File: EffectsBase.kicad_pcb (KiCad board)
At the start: 2 copper layers, 0 parts

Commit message: Initial schematic
Finished the base schematic.
Included all the controls and updated the power supply.
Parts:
- added REF**: Hammond_125B_1590N1_NOLID, Enclosures:Hammond_125B_1590N1_NOLID, B.Cu at (150.0, 100.0)
- added X1: PEDAL_COMBO_TOP, Custom_Parts:PEDAL_COMBO_TOP, F.Cu at (150.0, 44.0)
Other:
- board outline added: 59 x 95 mm
- copper layers 2 -> 4

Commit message: Initial layout
Finished the initial PCB layout.
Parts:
- removed X1: PEDAL_COMBO_TOP, Custom_Parts:PEDAL_COMBO_TOP
- added C1: 10u, Capacitor_SMD:C_0805_2012Metric, F.Cu at (94.8, 138.8)
- added C2: 10u, Capacitor_SMD:C_0805_2012Metric, F.Cu at (94.8, 141.2)
- added C3: 10n, Capacitor_SMD:C_0603_1608Metric, F.Cu at (87.2, 117.6)
- added C4: 10u, Capacitor_SMD:C_0805_2012Metric, F.Cu at (90.0, 134.4)
- added C5: 10u, Capacitor_SMD:C_0805_2012Metric, F.Cu at (90.0, 125.0)
- added C6: 10u, Capacitor_SMD:C_0805_2012Metric, F.Cu at (90.0, 127.8)
- added C7: 10u, Capacitor_SMD:C_0805_2012Metric, F.Cu at (90.0, 147.8)
- added C8: 10u, Capacitor_SMD:C_0805_2012Metric, F.Cu at (90.0, 145.6)
- added D1: SMF10CA, Diode_SMD:D_SOD-123F, F.Cu at (91.4, 117.6)
- added D2: MMSZ5248B, Diode_SMD:D_SOD-323, F.Cu at (88.0, 122.0)
- added D3: B5819W, Diode_SMD:D_SOD-123, F.Cu at (85.6, 140.0)
- added D4: H15VSD3B, Diode_SMD:D_SOD-323, F.Cu at (143.4, 67.2)
- added D5: H15VSD3B, Diode_SMD:D_SOD-323, F.Cu at (156.6, 67.2)
- added FB1: 850, Inductor_SMD:L_0603_1608Metric, F.Cu at (87.4, 126.4)
- added J1: JACK CONNECTOR, Custom_Parts:HEADER_THROUGH_2x03_P2.54mm, F.Cu at (150.0, 63.2)
- added J2: FOOTSWITCH, Custom_Parts:HEADER_THROUGH_2x06_P2.54mm, F.Cu at (150.0, 135.2)
- added J3: PCIE_FX, Custom_Parts:Mini PCI_Express, F.Cu at (150.0, 122.0)
- added Q1: SI2301BDS, Package_TO_SOT_SMD:SOT-23, F.Cu at (91.4, 122.0)
- added R1: 100, Resistor_SMD:R_0603_1608Metric, F.Cu at (90.0, 130.8)
- added R2: 4.7K, Resistor_SMD:R_0603_1608Metric, F.Cu at (89.2, 117.6)
- added RV1: RK09L, Custom_Parts:POT_SINGLE_VERTICAL_6X15, B.Cu at (170.0, 55.0)
- added RV2: RK09L, Custom_Parts:POT_SINGLE_VERTICAL_6X15, B.Cu at (150.0, 55.0)
- added RV3: RK09L, Custom_Parts:POT_SINGLE_VERTICAL_6X15, B.Cu at (130.0, 55.0)
- added RV4: RK09L, Custom_Parts:POT_SINGLE_VERTICAL_6X15, B.Cu at (150.0, 83.0)
- added SW1: SW_SPDT, Custom_Parts:SW_SPDT, B.Cu at (170.0, 83.0)
- added SW2: SW_SPDT, Custom_Parts:SW_SPDT, B.Cu at (130.0, 83.0)
- added SW3: MINI_SW, Custom_Parts:MINI_TOGGLE_SHIELD, B.Cu at (139.0, 105.0)
- added SW4: MINI_SW, Custom_Parts:MINI_TOGGLE_SHIELD, B.Cu at (161.0, 105.0)
- added U1: ICL7660S, Package_SO:SOIC-8_3.9x4.9mm_P1.27mm, F.Cu at (90.0, 140.0)
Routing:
- net /Controls/AUDIO_OUT: track 0.00 -> 100.1 mm, vias 0 -> 1
- net /Controls/AUDIO_IN: track 0.00 -> 100.1 mm, vias 0 -> 1
- net GND: track 0.00 -> 63.6 mm
- net +VCC_FILT: track 0.00 -> 19.2 mm
- net /Controls/FX_IN: track 0.00 -> 15.9 mm, vias 0 -> 2
- net /Controls/FX_OUT: track 0.00 -> 15.8 mm, vias 0 -> 2
- net /Controls/SW3_IN: track 0.00 -> 3.40 mm
- added copper zone on F.Cu, net +VCC
- added copper zone on F.Cu, net +VCC_FILT
- added copper zone on F.Cu, net +VDC
- added copper zone on F.Cu, net +VDC_PROT
- added copper zone on F.Cu, net -VSS
- added copper zone on F.Cu, net /Power/CAP+
- added copper zone on F.Cu, net /Power/CAP-
- added copper zone on F.Cu, net /Power/VG
- added copper zone on B.Cu, net GND
- added copper zone on F.Cu, net GND
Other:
- board size 59 x 95 mm -> 59 x 98 mm
- copper layers 4 -> 2
- board text added: "FOOTSWITCH 1"
- board text added: "FOOTSWITCH 2"

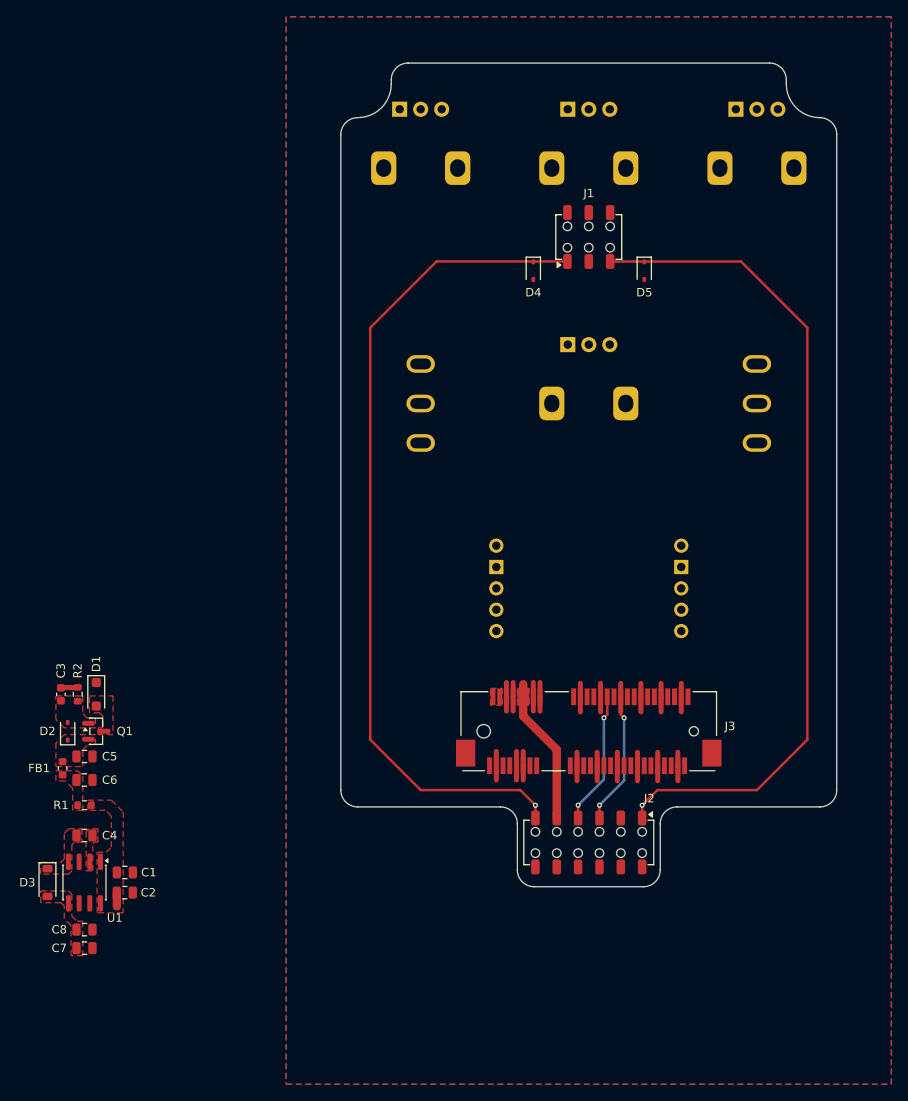
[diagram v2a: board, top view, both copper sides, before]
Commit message: Filtering section and layout
Updated the PCB layout.
Added additional input voltage filtering.
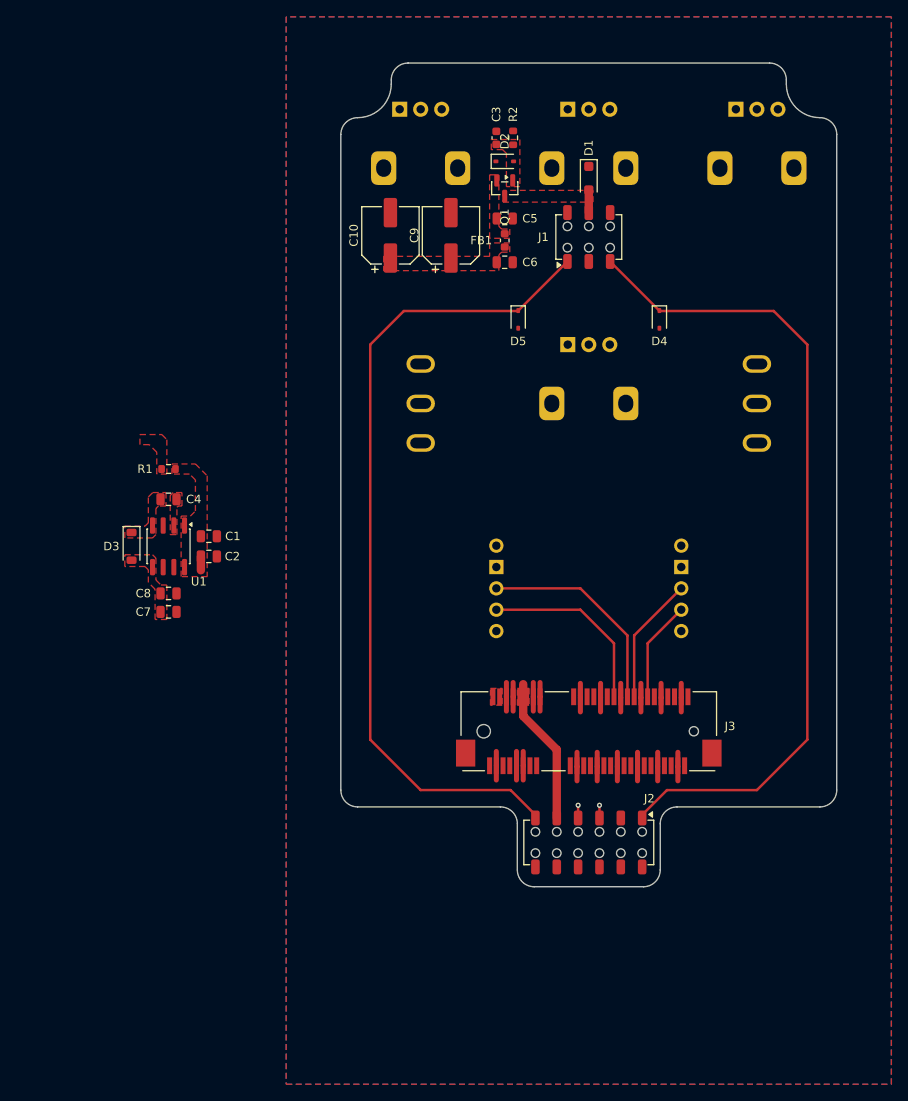
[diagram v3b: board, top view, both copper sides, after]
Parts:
- removed REF**: Hammond_125B_1590N1_NOLID, Enclosures:Hammond_125B_1590N1_NOLID
- added C10: 100u, Capacitor_SMD:CP_Elec_6.3x5.8, F.Cu at (126.4, 63.0)
- added C9: 100u, Capacitor_SMD:CP_Elec_6.3x5.8, F.Cu at (133.6, 63.0)
- moved D2 85.4 mm to (140.0, 54.2), turned to 0 degrees
- moved D1 84.9 mm to (150.0, 56.2)
- moved C3 84.1 mm to (139.0, 51.4)
- moved R2 84.1 mm to (141.0, 51.4)
- moved FB1 81.9 mm to (140.0, 63.6)
- moved C5 81.2 mm to (140.0, 61.0)
- moved Q1 80.8 mm to (140.0, 57.4), turned to -90 degrees
- moved C6 79.3 mm to (140.0, 66.2)
- moved C1 41.2 mm to (104.8, 98.8)
- moved C7 41.2 mm to (100.0, 107.8)
- moved R1 41.2 mm to (100.0, 90.8)
- moved C4 41.2 mm to (100.0, 94.4)
- moved C8 41.2 mm to (100.0, 105.6)
- moved D3 41.2 mm to (95.6, 100.0)
- moved U1 41.2 mm to (100.0, 100.0)
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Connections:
- J3 pad 30: /Controls/SW3_IN -> /Controls/SW3_NO
- J3 pad 34: /Controls/SW3_NO -> /Controls/SW3_IN
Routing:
- net /Controls/SW3_NO: track 0.00 -> 22.0 mm
- net /Controls/SW3_IN: track 3.40 -> 25.2 mm
- net /Controls/SW4_IN: track 0.00 -> 15.2 mm
- net /Controls/FX_IN: track 15.9 -> 1.52 mm, vias 2 -> 1
- net /Controls/FX_OUT: track 15.8 -> 1.52 mm, vias 2 -> 1
- net /Controls/SW4_NO: track 0.00 -> 12.0 mm
- net +VDC: track 0.00 -> 2.69 mm
- net /Controls/AUDIO_IN: track 100.1 -> 98.3 mm, vias 1 -> 0
- net /Controls/AUDIO_OUT: track 100.1 -> 98.3 mm, vias 1 -> 0
- net GND: track 63.6 -> 65.1 mm

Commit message: Charge pump layout
Added the layout for the charge pump.
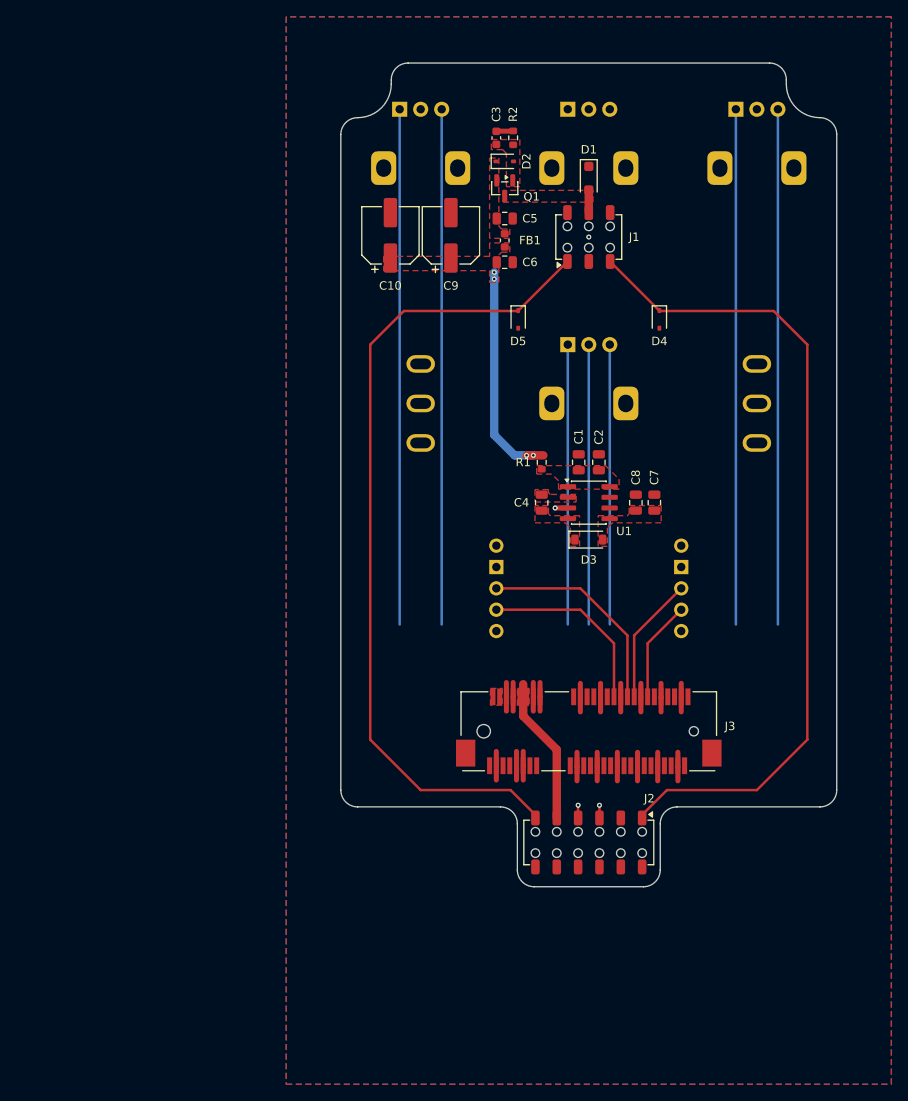
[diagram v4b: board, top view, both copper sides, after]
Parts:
- moved C7 59.2 mm to (157.8, 94.8), turned to 90 degrees
- moved C8 56.6 mm to (155.6, 94.8), turned to 90 degrees
- moved D3 54.4 mm to (150.0, 99.2), turned to 0 degrees
- moved U1 50.3 mm to (150.0, 94.8), turned to 0 degrees
- moved C2 47.7 mm to (151.2, 90.0), turned to 90 degrees
- moved C1 44.9 mm to (148.8, 90.0), turned to 90 degrees
- moved R1 44.4 mm to (144.4, 90.0), turned to -90 degrees
- moved C4 44.4 mm to (144.4, 94.8), turned to -90 degrees
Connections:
- C3 pad 2: GND -> +VCC
- J3 pad 11: GND -> +VCC
- J3 pad 14: GND -> +VCC
- J3 pad 16: GND -> +VCC
- J3 pad 19: GND -> +VCC
- J3 pad 20: GND -> +VCC
- J3 pad 25: GND -> +VCC
- J3 pad 26: GND -> +VCC
- J3 pad 3: GND -> +VCC
- J3 pad 31: GND -> +VCC
- J3 pad 32: GND -> +VCC
- J3 pad 37: GND -> +VCC
- J3 pad 38: GND -> +VCC
- J3 pad 43: GND -> +VCC
- J3 pad 44: GND -> +VCC
- J3 pad 49: GND -> +VCC
- J3 pad 50: GND -> +VCC
- J3 pad 6: GND -> +VCC
- J3 pad 8: GND -> +VCC
- J3 pad 9: GND -> +VCC
- R2 pad 2: GND -> +VCC
- U1 pad 3: GND -> +VCC
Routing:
- net +VCC: track 0.00 -> 95.6 mm, vias 0 -> 4
- net GND: track 65.1 -> 0.00 mm, vias 0 -> 2
- net /Controls/P3_L: track 0.00 -> 61.3 mm
- net /Controls/P3_H: track 0.00 -> 61.3 mm
- net /Controls/P1_L: track 0.00 -> 61.3 mm
- net /Controls/P1_H: track 0.00 -> 61.3 mm
- net /Controls/P4_W: track 0.00 -> 33.3 mm
- net /Controls/P4_L: track 0.00 -> 33.3 mm
- net /Controls/P4_H: track 0.00 -> 33.3 mm
- net +VCC_FILT: track 19.2 -> 17.6 mm

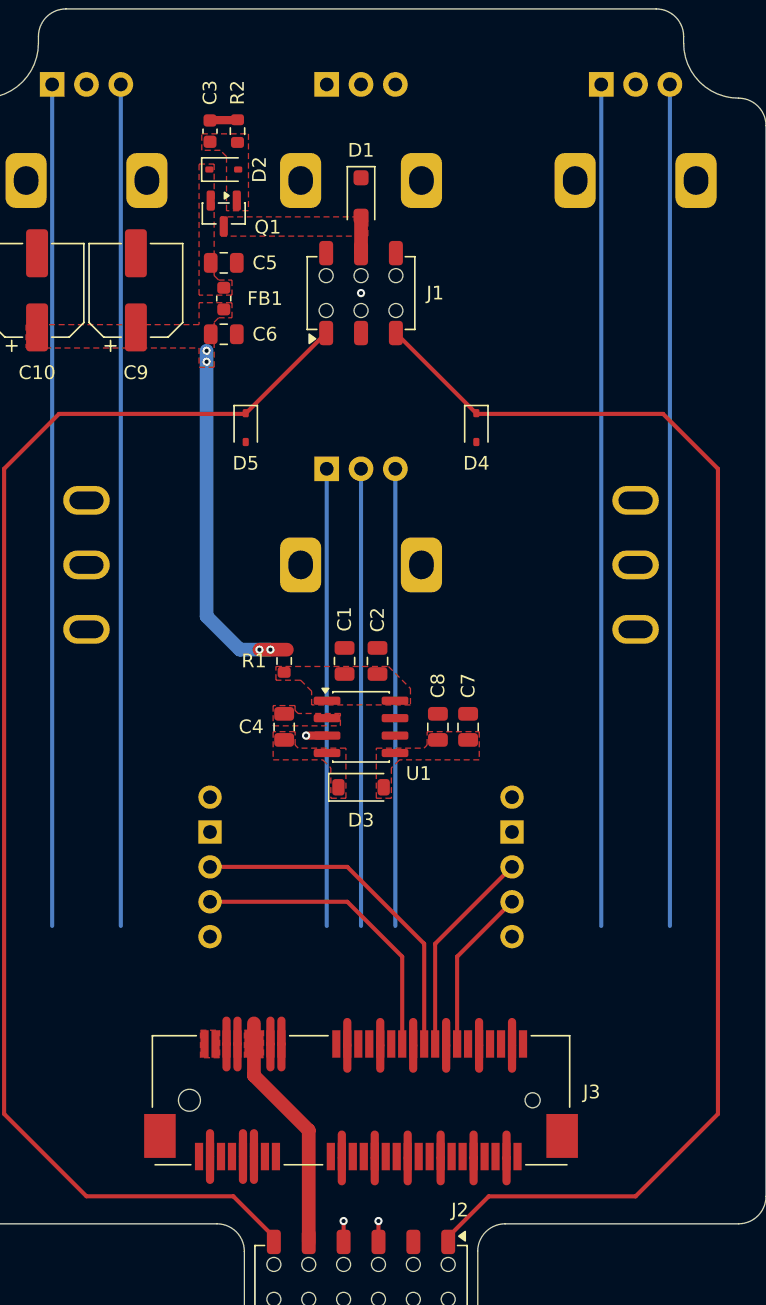
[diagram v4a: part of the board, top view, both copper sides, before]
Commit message: Control layout
Updated the layout for the controls.
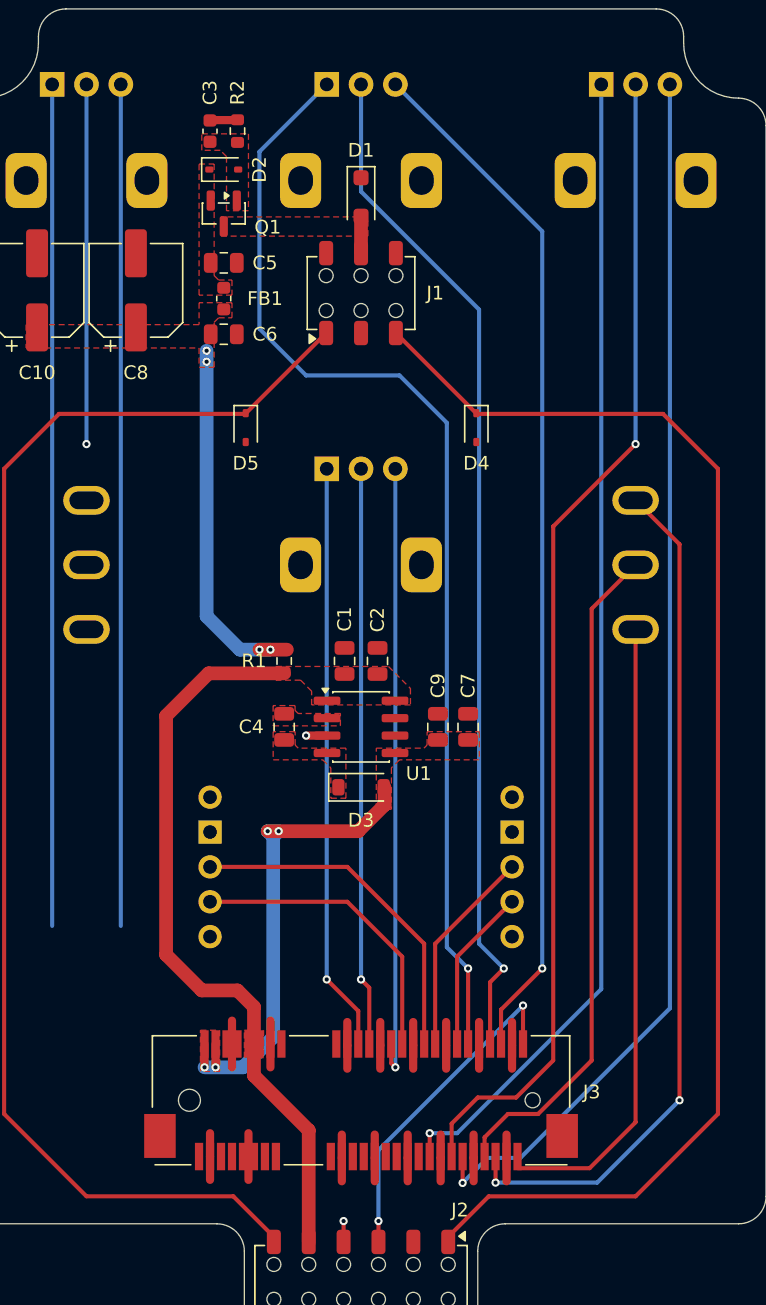
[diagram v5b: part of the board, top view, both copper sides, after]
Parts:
- moved RV1 40.0 mm to (130.0, 55.0)
- moved SW1 40.0 mm to (130.0, 83.0)
- moved SW2 40.0 mm to (170.0, 83.0)
- moved RV3 34.4 mm to (150.0, 83.0)
- moved RV4 28.0 mm to (150.0, 55.0)
- moved RV2 20.0 mm to (170.0, 55.0)
- renumbered C9 to C8, C8 to C9
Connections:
- C3 pad 2: +VCC -> GND
- J3 pad 11: +VCC -> GND
- J3 pad 14: +VCC -> GND
- J3 pad 16: +VCC -> GND
- J3 pad 19: +VCC -> GND
- J3 pad 20: +VCC -> GND
- J3 pad 25: +VCC -> GND
- J3 pad 26: +VCC -> GND
- J3 pad 3: +VCC -> GND
- J3 pad 31: +VCC -> GND
- J3 pad 32: +VCC -> GND
- J3 pad 37: +VCC -> GND
- J3 pad 38: +VCC -> GND
- J3 pad 43: +VCC -> GND
- J3 pad 44: +VCC -> GND
- J3 pad 49: +VCC -> GND
- J3 pad 50: +VCC -> GND
- J3 pad 6: +VCC -> GND
- J3 pad 8: +VCC -> GND
- J3 pad 9: +VCC -> GND
- R2 pad 2: +VCC -> GND
- U1 pad 3: +VCC -> GND
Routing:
- net /Controls/P2_L: track 0.00 -> 89.6 mm, vias 0 -> 1
- net /Controls/P2_W: track 0.00 -> 85.3 mm, vias 0 -> 1
- net /Controls/P2_H: track 0.00 -> 84.4 mm, vias 0 -> 1
- net +VCC: track 95.6 -> 27.0 mm
- net /Controls/SW2_NC: track 0.00 -> 62.8 mm, vias 0 -> 2
- net GND: track 0.00 -> 58.4 mm, vias 2 -> 1
- net /Controls/SW2_IN: track 0.00 -> 48.9 mm
- net /Controls/P4_H: track 33.3 -> 82.2 mm, vias 0 -> 1
- net /Controls/SW2_NO: track 0.00 -> 46.6 mm
- net /Controls/P4_L: track 33.3 -> 75.6 mm, vias 0 -> 1
- net /Controls/P3_W: track 0.00 -> 42.1 mm, vias 0 -> 1
- net /Controls/P4_W: track 33.3 -> 74.6 mm, vias 0 -> 1
- net +VCC_FILT: track 17.6 -> 54.0 mm
- net -VSS: track 0.00 -> 36.4 mm, vias 0 -> 4
- net /Controls/P1_W: track 0.00 -> 26.2 mm, vias 0 -> 1
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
